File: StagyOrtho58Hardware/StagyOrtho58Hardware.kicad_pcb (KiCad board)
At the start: 2 copper layers, 185.9 x 130 mm, 83 parts, among them J11 USB_C_Receptacle_USB2.0, SW11 SW_Push, SW12 SW_Push, SW13 SW_Push, SW14 SW_Push, SW15 SW_Push, SW16 SW_Push, SW17 SW_Push, SW18 SW_Push, SW19 SW_Push, SW20 SW_Push, SW21 SW_Push, SW22 SW_Push, SW23 SW_Push, SW24 SW_Push, SW25 SW_Push, SW26 SW_Push, SW27 SW_Push, SW28 SW_Push, SW29 SW_Push, SW30 SW_Push, SW31 SW_Push, SW32 SW_Push, SW33 SW_Push, SW34 SW_Push, SW35 SW_Push, SW36 SW_Push, SW37 SW_Push, SW38 SW_Push, SW39 SW_Push, SW40 SW_Push, U11 Pico, U12 MCP23S17_ML

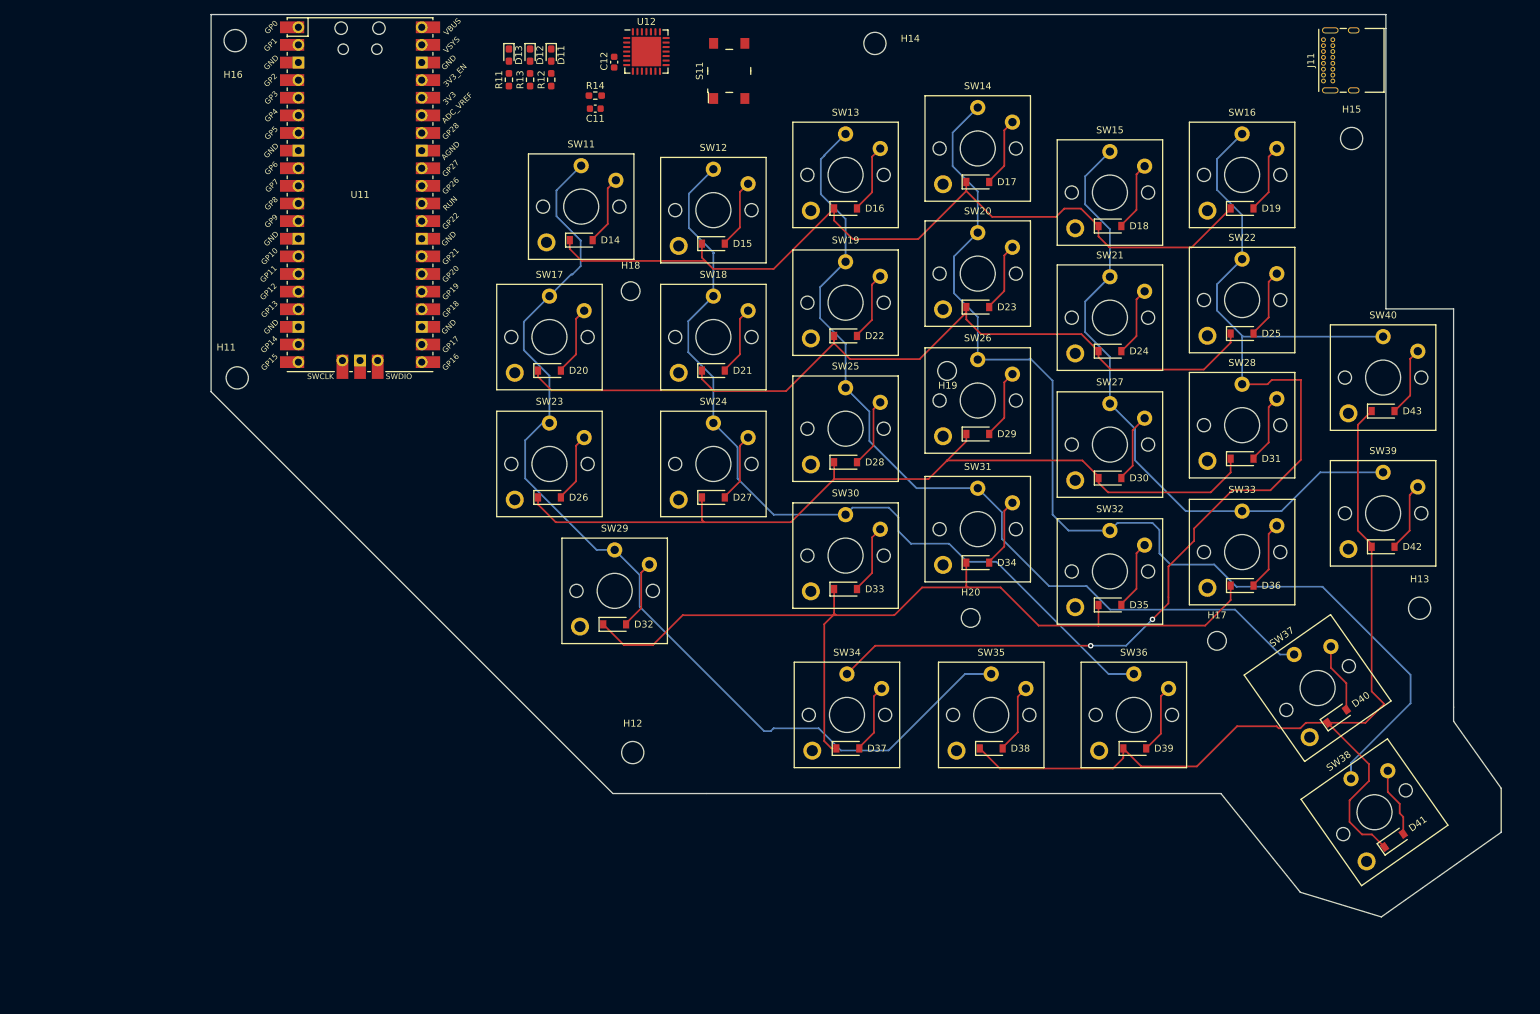
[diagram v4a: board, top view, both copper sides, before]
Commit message: Completes routing of the board
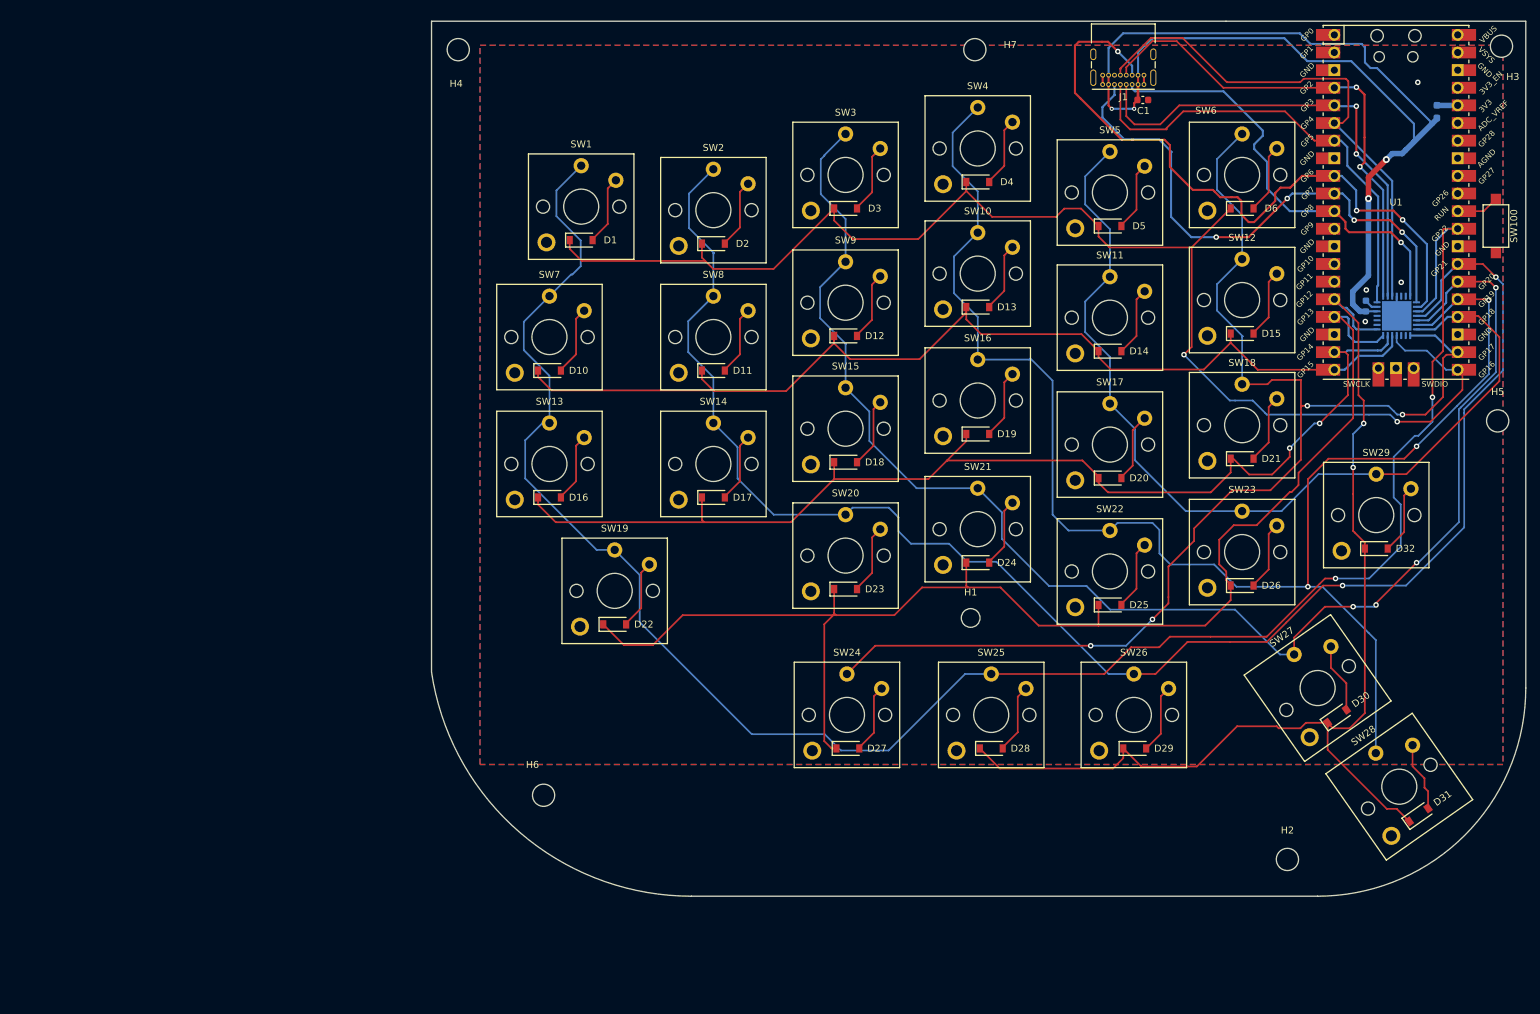
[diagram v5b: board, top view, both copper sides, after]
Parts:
- removed C12: C, Capacitor_SMD:C_0603_1608Metric
- removed the D11 at (111.3, 39.9)
- removed the D12 at (108.2, 39.9)
- removed the D13 at (105.2, 39.9)
- removed D43: 1N4148W, Diode_SMD:D_SOD-123
- removed H17, H18, H19: MountingHole, MountingHole:MountingHole_2.7mm_M2.5
- removed R11, R12, R13: 200, Resistor_SMD:R_0603_1608Metric_Pad0.98x0.95mm_HandSolder
- removed R14: 0, Resistor_SMD:R_0603_1608Metric_Pad0.98x0.95mm_HandSolder
- removed S11: PTS645SM43SMTR92_LFS, digikey-footprints:Switch_Tactile_SMD_6x6mm_PTS645
- removed SW40: SW_Push, Switch_Keyboard_Kailh:SW_Kailh_Choc_V1V2_1.00u
- removed U11: Pico, MCU_RaspberryPi_and_Boards:RPi_Pico_SMD_TH
- removed U12: MCP23S17_ML, Package_DFN_QFN:QFN-28-1EP_6x6mm_P0.65mm_EP4.25x4.25mm
- added C2: C, Capacitor_SMD:C_0603_1608Metric, B.Cu at (228.7, 76.0)
- added R1: 0, Resistor_SMD:R_0603_1608Metric_Pad0.98x0.95mm_HandSolder, B.Cu at (238.9, 48.0)
- added SW100: SW_SPST, Button_Switch_SMD:SW_SPST_CK_RS282G05A3, F.Cu at (247.4, 64.5)
- added U1: Pico, MCU_RaspberryPi_and_Boards:RPi_Pico_SMD_TH, F.Cu at (233.0, 61.1)
- added U2: MCP23S17_ML, Package_DFN_QFN:QFN-28-1EP_6x6mm_P0.65mm_EP4.25x4.25mm, B.Cu at (233.1, 77.5)
- moved H5 133.5 mm to (247.7, 92.6)
- moved C1 78.9 mm to (196.5, 46.4), turned to 0 degrees
- moved H6 74.6 mm to (110.2, 146.6)
- moved H2 40.9 mm to (217.3, 155.8)
- moved H4 32.2 mm to (97.8, 39.1)
- moved J1 25.9 mm to (196.7, 44.1), turned to 180 degrees
- moved H3 25.4 mm to (248.2, 38.6)
- moved H7 14.4 mm to (172.3, 39.1)
- moved D31 5.13 mm to (236.3, 149.4)
- moved SW28 5.13 mm to (233.5, 145.3)
- moved D32 1.02 mm to (230.2, 111.0)
- moved SW29 1.02 mm to (230.2, 106.2)
- renumbered C11 to C1, D14 to D1, D20 to D10, D21 to D11, D22 to D12, D23 to D13, D24 to D14, D25 to D15, D26 to D16, D27 to D17, D28 to D18, D29 to D19, D15 to D2, D30 to D20, D31 to D21, D32 to D22, D33 to D23, D34 to D24, D35 to D25, D36 to D26, D37 to D27, D38 to D28, D39 to D29, D16 to D3, D40 to D30, D41 to D31, D42 to D32, D17 to D4, D18 to D5, D19 to D6, H20 to H1, H13 to H2, H15 to H3, H16 to H4, H12 to H5, H11 to H6, H14 to H7, J11 to J1, SW11 to SW1, SW20 to SW10, SW21 to SW11, SW22 to SW12, SW23 to SW13, SW24 to SW14, SW25 to SW15, SW26 to SW16, SW27 to SW17, SW28 to SW18, SW29 to SW19, SW12 to SW2, SW30 to SW20, SW31 to SW21, SW32 to SW22, SW33 to SW23, SW34 to SW24, SW35 to SW25, SW36 to SW26, SW37 to SW27, SW38 to SW28, SW39 to SW29, SW13 to SW3, SW14 to SW4, SW15 to SW5, SW16 to SW6, SW17 to SW7, SW18 to SW8, SW19 to SW9
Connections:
- J1 pad B5: /GREEN -> unconnected-(J1-PadB5)
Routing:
- net +VDC: track 0.00 -> 159.8 mm, vias 0 -> 4
- net /COL_0: track 146.1 -> 280.9 mm, vias 0 -> 2
- net /COL_1: track 122.8 -> 234.9 mm, vias 0 -> 2
- net /INTA: track 0.00 -> 98.8 mm, vias 0 -> 3
- net /COL_2: track 127.9 -> 212.1 mm, vias 0 -> 4
- net /INTB: track 0.00 -> 78.5 mm, vias 0 -> 4
- net /ROW_0: track 118.6 -> 195.2 mm, vias 0 -> 2
- net /SPI0_RX: track 0.00 -> 74.6 mm
- net /SPI0_SCK: track 0.00 -> 71.0 mm, vias 0 -> 2
- net /SPI0_TX: track 0.00 -> 68.6 mm, vias 0 -> 2
- net /SPI0_CSn: track 0.00 -> 66.0 mm
- net /~{RESET}: track 0.00 -> 62.9 mm, vias 0 -> 1
- net /ROW_3: track 132.4 -> 193.8 mm
- net /COL_3: track 156.2 -> 217.4 mm, vias 0 -> 3
- net /COL_4: track 93.0 -> 135.6 mm
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- added copper zone on B.Cu, net GND
- added copper zone on F.Cu, net GND
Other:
- board size 185.9 x 130 mm -> 157.7 x 126.1 mm
